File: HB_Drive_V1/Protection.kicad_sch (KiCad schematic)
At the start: 54 parts, among them J701 Conn_02x02_Odd_Even, J702 Conn_02x02_Odd_Even, Q701 BSS138, Q702 BSS138, SW701 PTS636SL43SMTRLFS, SW704 PTS636SL43SMTRLFS, U402 74LS08, U702 74LS32, U703 TL082, U704 TL082, U705 LM311, U706 74LS02

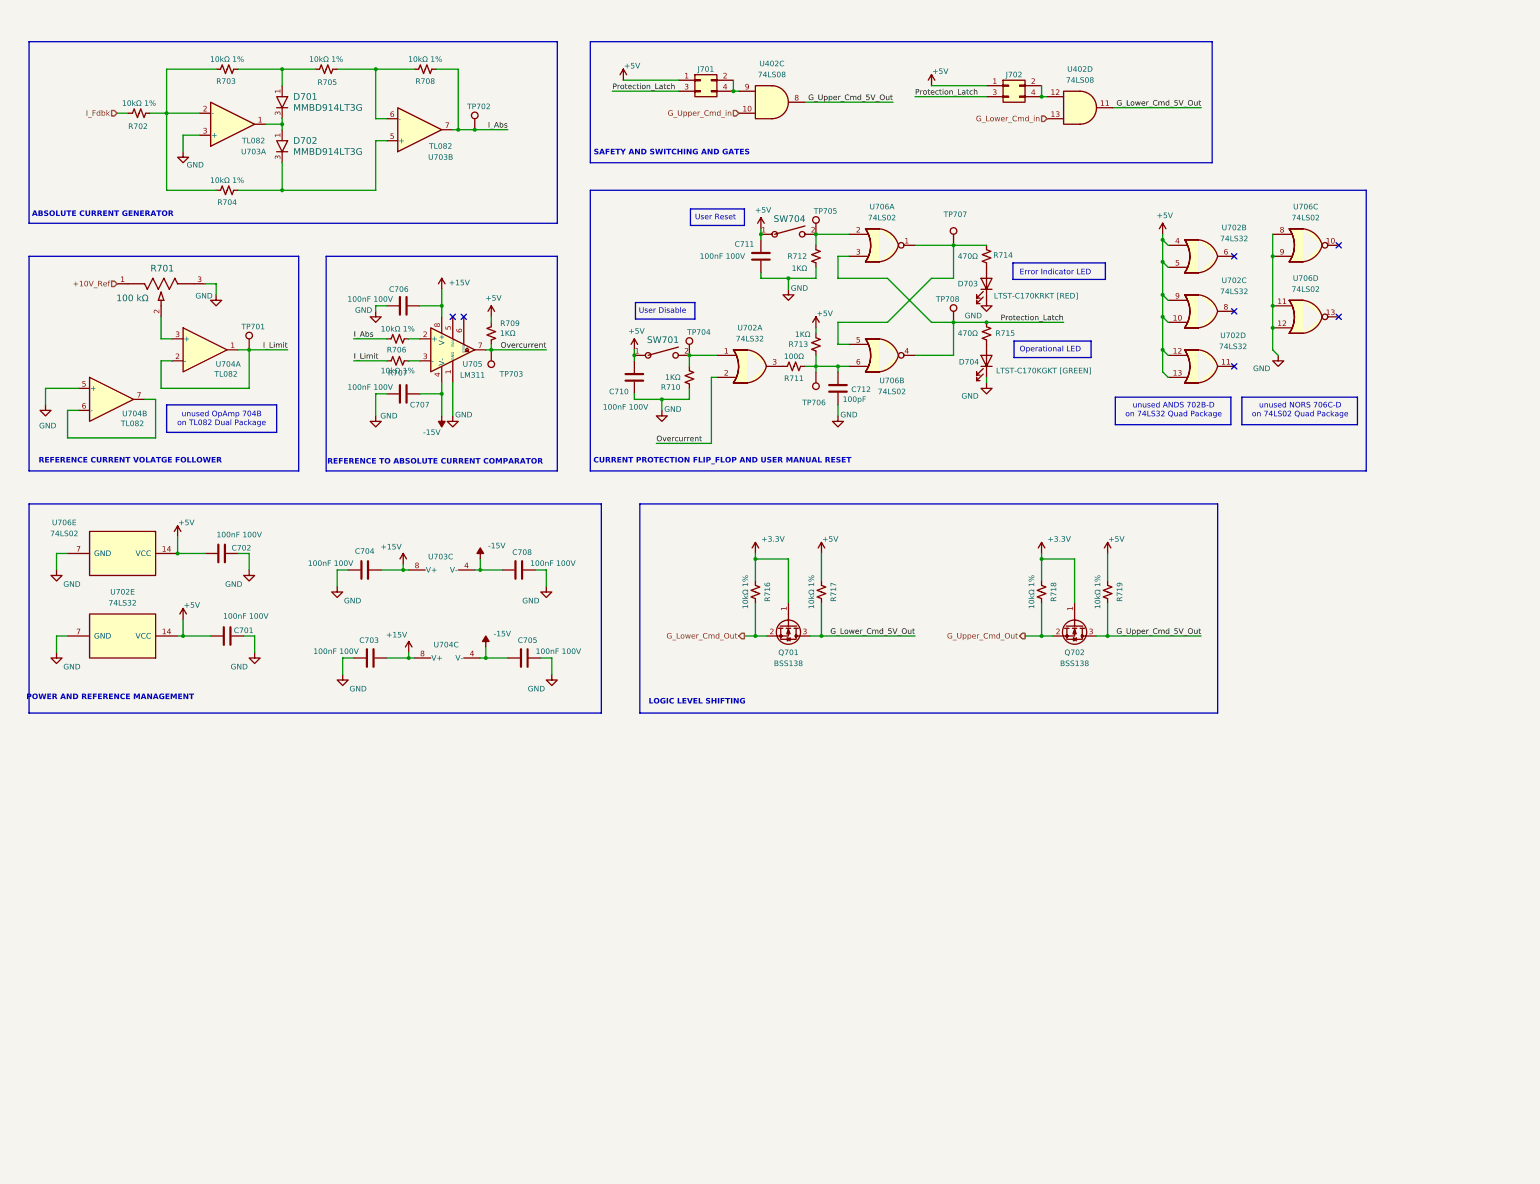
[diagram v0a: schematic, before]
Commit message: Makes annotation changes
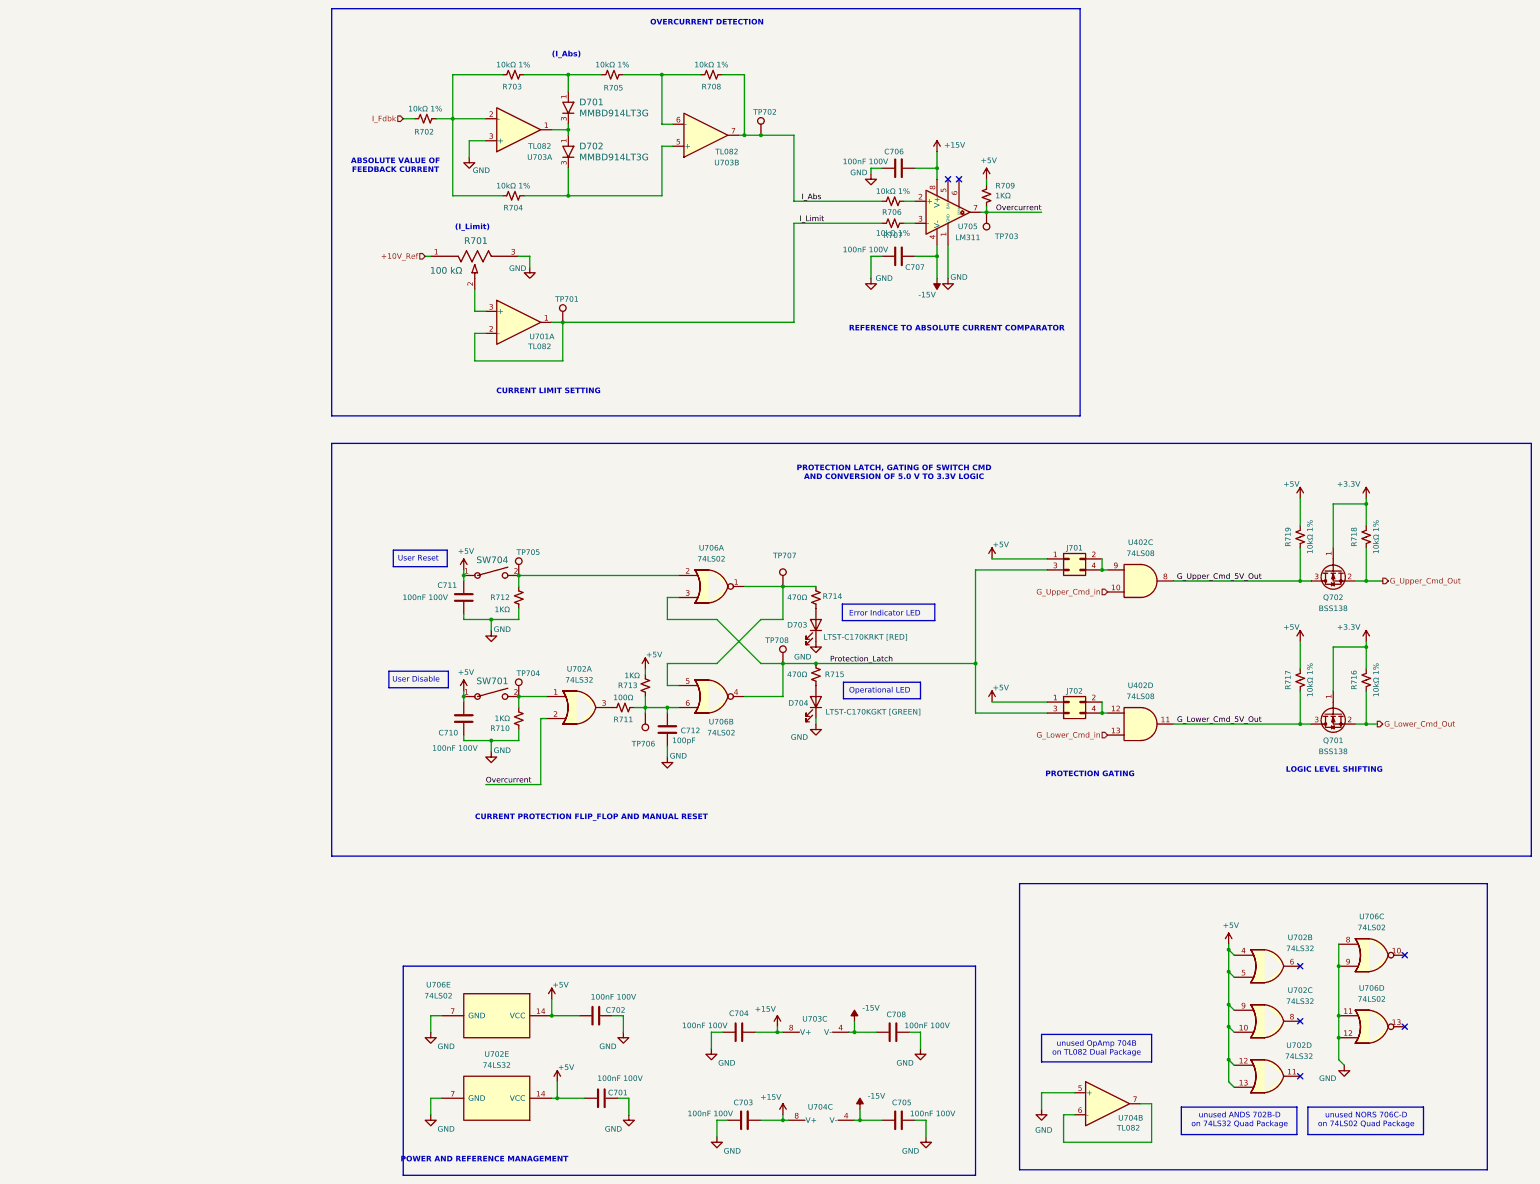
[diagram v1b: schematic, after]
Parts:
- removed unit 1 of U704
- added U701: TL082, Package_SO:SOIC-8_3.9x4.9mm_P1.27mm, symbol Amplifier_Operational:TL082
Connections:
- net I_Limit: now also U701.1, U701.2 (-)
- net at R701.2: now also U701.3 (+)
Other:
- note added: "(I_Abs)"
- note added: "(I_Limit)"
- note added: "ABSOLUTE VALUE OF FEEDBACK CURRENT"
- note added: "CURRENT LIMIT SETTING"
- note added: "CURRENT PROTECTION FLIP_FLOP AND MANUAL RESET"
- note added: "OVERCURRENT DETECTION"
- note added: "PROTECTION GATING"
- note added: "PROTECTION LATCH, GATING OF SWITCH CMD AND CONVERSION OF 5.0 V TO 3.3V LOGIC"
- note removed: "ABSOLUTE CURRENT GENERATOR"
- note removed: "CURRENT PROTECTION FLIP_FLOP AND USER MANUAL RESET"
- note removed: "REFERENCE CURRENT VOLATGE FOLLOWER"
- note removed: "SAFETY AND SWITCHING AND GATES"
- moved on the sheet: C701, C702, C703, C704, C705, C708, C710, C711, C712, D703, D704, J701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
